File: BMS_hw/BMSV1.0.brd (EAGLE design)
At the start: 272 x 60 mm, 161 parts, among them IC1 MC33771BEP, IC2 SFH6156, J2 NTC, X2 87758-1816

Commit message: updated after nxp review
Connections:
- removed net N$28: C67.1, IC1.43
- new net N$14: IC1.45, IC1.48
- net GND: no longer R66.2
- net VCOM: now also C67.1, IC1.43, R66.2
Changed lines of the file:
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@@
 <contactref element="C67" pad="2"/>
 <contactref element="IC2" pad="2"/>
-<contactref element="R66" pad="2"/>
 <contactref element="R67" pad="2"/>
 <contactref element="X2" pad="11"/>
@@
 <wire x1="-96.94" y1="19.05" x2="-81.7" y2="38.1" width="0" layer="19" extent="1-1"/>
 <wire x1="-30.75" y1="76.2" x2="-48.68" y2="50.8" width="0" layer="19" extent="1-1"/>
-<wire x1="-25.67" y1="76.2" x2="-30.75" y2="76.2" width="0" layer="19" extent="1-1"/>
 <wire x1="29.27" y1="36.41" x2="-18.2" y2="25.4" width="0" layer="19" extent="1-1"/>
 <wire x1="-20.825" y1="-100.33" x2="-79.58" y2="-95.25" width="0" layer="19" extent="1-1"/>
@@
 <contactref element="R97" pad="2"/>
 <contactref element="R98" pad="2"/>
+<contactref element="C67" pad="1"/>
+<contactref element="IC1" pad="43"/>
+<contactref element="R66" pad="2"/>
 <wire x1="-75.2" y1="-68.58" x2="-80.28" y2="-68.58" width="0" layer="19" extent="1-1"/>
 <wire x1="-70.12" y1="-68.58" x2="-75.2" y2="-68.58" width="0" layer="19" extent="1-1"/>
@@
 <wire x1="-54.88" y1="-68.58" x2="-59.96" y2="-68.58" width="0" layer="19" extent="1-1"/>
 <wire x1="-49.8" y1="-68.58" x2="-54.88" y2="-68.58" width="0" layer="19" extent="1-1"/>
+<wire x1="-56.73" y1="50.8" x2="-54.88" y2="-68.58" width="0" layer="19" extent="1-1"/>
+<wire x1="-25.67" y1="76.2" x2="-56.73" y2="50.8" width="0" layer="19" extent="1-1"/>
+<wire x1="38.95" y1="31.73" x2="-25.67" y2="76.2" width="0" layer="19" extent="1-1"/>
 </signal>
 <signal name="GPIO0">
@@
 <contactref element="C66" pad="1"/>
 <wire x1="-50.38" y1="50.8" x2="31.27" y2="36.41" width="0" layer="19" extent="1-1"/>
-</signal>
-<signal name="N$28">
-<contactref element="C67" pad="1"/>
-<contactref element="IC1" pad="43"/>
-<wire x1="-56.73" y1="50.8" x2="38.95" y2="31.73" width="0" layer="19" extent="1-1"/>
 </signal>
 <signal name="VPWR">
@@
 <contactref element="R7" pad="1"/>
 </signal>
+<signal name="N$14">
+<contactref element="IC1" pad="45"/>
+<contactref element="IC1" pad="48"/>
+<wire x1="38.95" y1="32.73" x2="38.95" y2="34.23" width="0" layer="19" extent="1-1"/>
+</signal>
 </signals>

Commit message: cell terminal pads are placed according to design
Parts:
- CELL1+, CELL1-, CELL10+, CELL11+, CELL12+, CELL13+, CELL14+, CELL2+, CELL3+, CELL4+, CELL5+, CELL6+, CELL7+, CELL8+, CELL9+: value TPSQTP20SQ -> GF_BMS_CELL_PADP_PAD; device testpad:TP20SQ -> GreenFuel:GF-BMS-PAD
- moved CELL14+ 329.2 mm to (259.5, 54.0)
- moved CELL13+ 309.5 mm to (240.5, 6.00)
- moved CELL12+ 292.6 mm to (240.5, 54.0)
- moved CELL11+ 289.9 mm to (202.5, 6.00)
- moved CELL8+ 265.7 mm to (164.5, 54.0)
- moved CELL6+ 257.6 mm to (126.5, 54.0)
- moved CELL10+ 245.9 mm to (202.5, 54.0)
- moved CELL7+ 227.7 mm to (126.5, 6.00)
- moved CELL5+ 209.2 mm to (88.5, 6.00)
- moved CELL9+ 203.0 mm to (164.5, 6.00)
- moved CELL4+ 188.9 mm to (88.5, 54.0)
- moved CELL2+ 174.6 mm to (50.5, 54.0)
- moved CELL1- 161.1 mm to (12.5, 54.0)
- moved CELL3+ 135.7 mm to (50.5, 6.00)
- moved CELL1+ 120.1 mm to (12.5, 6.00)
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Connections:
- net CB_10/9_C: now also CELL9+.1; no longer CELL9+.TP
- net CB_12/11_C: now also CELL11+.1; no longer CELL11+.TP
- net CB_13/12_C: now also CELL12+.1; no longer CELL12+.TP
- net CB_13/12_C1: now also CELL10+.1; no longer CELL10+.TP
- net CB_13/12_C2: now also CELL8+.1; no longer CELL8+.TP
- net CB_13/12_C6: now also CELL6+.1; no longer CELL6+.TP
- net CB_13/12_C7: now also CELL4+.1; no longer CELL4+.TP
- net CB_13/12_C8: now also CELL2+.1; no longer CELL2+.TP
- net CB_14/13_C: now also CELL13+.1; no longer CELL13+.TP
- net CB_2/1_C: now also CELL1+.1; no longer CELL1+.TP
- net CB_4/3_C: now also CELL3+.1; no longer CELL3+.TP
- net CB_6/5_C: now also CELL5+.1; no longer CELL5+.TP
- net CB_8/7_C: now also CELL7+.1; no longer CELL7+.TP
- net CELL1-: now also CELL1-.1; no longer CELL1-.TP
- net CELL14+: now also CELL14+.1; no longer CELL14+.TP
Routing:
- added copper zone on layer 16, net GND

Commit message: board updated cell name and value
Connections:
- net CB_10/9_C: now also CELL9+.P$1; no longer CELL9+.1
- net CB_12/11_C: now also CELL11+.P$1; no longer CELL11+.1
- net CB_13/12_C: now also CELL12+.P$1; no longer CELL12+.1
- net CB_13/12_C1: now also CELL10+.P$1; no longer CELL10+.1
- net CB_13/12_C2: now also CELL8+.P$1; no longer CELL8+.1
- net CB_13/12_C6: now also CELL6+.P$1; no longer CELL6+.1
- net CB_13/12_C7: now also CELL4+.P$1; no longer CELL4+.1
- net CB_13/12_C8: now also CELL2+.P$1; no longer CELL2+.1
- net CB_14/13_C: now also CELL13+.P$1; no longer CELL13+.1
- net CB_2/1_C: now also CELL1+.P$1; no longer CELL1+.1
- net CB_4/3_C: now also CELL3+.P$1; no longer CELL3+.1
- net CB_6/5_C: now also CELL5+.P$1; no longer CELL5+.1
- net CB_8/7_C: now also CELL7+.P$1; no longer CELL7+.1
- net CELL1-: now also CELL1-.P$1; no longer CELL1-.1
- net CELL14+: now also CELL14+.P$1; no longer CELL14+.1
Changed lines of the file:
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@@
 </elements>
 <signals>
-<signal name="N$1">
-<contactref element="R26" pad="2"/>
-<contactref element="R31" pad="1"/>
-<contactref element="C27" pad="1"/>
-<wire x1="-42.76" y1="44.45" x2="-91.71" y2="57.15" width="0" layer="19" extent="1-1"/>
-<wire x1="-32.75" y1="63.5" x2="-42.76" y2="44.45" width="0" layer="19" extent="1-1"/>
-</signal>
 <signal name="GND">
 <contactref element="C27" pad="2"/>
@@
 <contactref element="C20" pad="2"/>
 <contactref element="C4" pad="2"/>
-<contactref element="C21" pad="2"/>
 <contactref element="IC1" pad="65"/>
 <contactref element="IC1" pad="58"/>
@@
 <vertex x="0" y="48"/>
 </polygon>
+<contactref element="C21" pad="2"/>
 <wire x1="-94.4" y1="-107.95" x2="-100.75" y2="-107.95" width="0" layer="19" extent="1-1"/>
 <wire x1="-88.05" y1="-107.95" x2="-94.4" y2="-107.95" width="0" layer="19" extent="1-1"/>
@@
 <contactref element="C10" pad="1"/>
 <contactref element="R17" pad="1"/>
-<contactref element="CELL13+" pad="1"/>
+<contactref element="CELL13+" pad="P$1"/>
 <wire x1="-37.68" y1="25.4" x2="240.5" y2="6" width="0" layer="19" extent="1-1"/>
 <wire x1="-47.99" y1="57.15" x2="-37.68" y2="25.4" width="0" layer="19" extent="1-1"/>
@@
 <contactref element="R6" pad="1"/>
 <contactref element="R9" pad="1"/>
-<contactref element="CELL12+" pad="1"/>
+<contactref element="CELL12+" pad="P$1"/>
 <wire x1="-22.59" y1="82.55" x2="-17.51" y2="82.55" width="0" layer="19" extent="1-1"/>
 <wire x1="-63.08" y1="19.05" x2="-22.59" y2="82.55" width="0" layer="19" extent="1-1"/>
@@
 <contactref element="C11" pad="1"/>
 <contactref element="R18" pad="1"/>
-<contactref element="CELL11+" pad="1"/>
+<contactref element="CELL11+" pad="P$1"/>
 <contactref element="IC1" pad="10"/>
 <wire x1="39.91" y1="29.73" x2="202.5" y2="6" width="0" layer="19" extent="1-16"/>
@@
 <contactref element="R4" pad="1"/>
 <contactref element="R14" pad="1"/>
-<contactref element="CELL10+" pad="1"/>
+<contactref element="CELL10+" pad="P$1"/>
 <wire x1="-32.75" y1="57.15" x2="-17.51" y2="63.5" width="0" layer="19" extent="1-1"/>
 <wire x1="-19.9" y1="25.4" x2="-32.75" y2="57.15" width="0" layer="19" extent="1-1"/>
@@
 <wire x1="-51.07" y1="63.5" x2="-37.68" y2="31.75" width="0" layer="19" extent="1-1"/>
 </signal>
-<signal name="N$8">
-<contactref element="R20" pad="2"/>
-<contactref element="R37" pad="1"/>
-<contactref element="C21" pad="1"/>
-<wire x1="-61.23" y1="57.15" x2="-83.4" y2="38.1" width="0" layer="19" extent="1-1"/>
-<wire x1="-63.23" y1="63.5" x2="-61.23" y2="57.15" width="0" layer="19" extent="1-1"/>
-</signal>
 <signal name="CB_13/12_C2">
 <contactref element="C4" pad="1"/>
@@
 <contactref element="R2" pad="1"/>
 <contactref element="R10" pad="1"/>
-<contactref element="CELL8+" pad="1"/>
+<contactref element="CELL8+" pad="P$1"/>
 <wire x1="-17.51" y1="57.15" x2="164.5" y2="54" width="0" layer="19" extent="1-1"/>
 <wire x1="-63.23" y1="57.15" x2="-17.51" y2="57.15" width="0" layer="19" extent="1-1"/>
@@
 </signal>
 <signal name="CT_8">
+<contactref element="C36" pad="2"/>
+<contactref element="IC1" pad="18"/>
 <contactref element="R37" pad="2"/>
 <contactref element="C37" pad="1"/>
-<contactref element="C36" pad="2"/>
-<contactref element="IC1" pad="18"/>
 <wire x1="-44.87" y1="31.75" x2="37.23" y2="24.55" width="0" layer="19" extent="1-16"/>
 <wire x1="-55.46" y1="31.75" x2="-44.87" y2="31.75" width="0" layer="19" extent="1-1"/>
@@
 <contactref element="C71" pad="1"/>
 <contactref element="R46" pad="1"/>
-<contactref element="CELL7+" pad="1"/>
+<contactref element="CELL7+" pad="P$1"/>
 <contactref element="D10" pad="A"/>
 <wire x1="-77.2" y1="-55.88" x2="-99.9" y2="-95.25" width="0" layer="19" extent="1-1"/>
@@
 </signal>
 <signal name="CT_7">
+<contactref element="IC1" pad="22"/>
 <contactref element="C37" pad="2"/>
-<contactref element="IC1" pad="22"/>
 <wire x1="-53.76" y1="31.75" x2="35.23" y2="24.55" width="0" layer="19" extent="1-16"/>
 </signal>
@@
 <contactref element="C75" pad="1"/>
 <contactref element="R73" pad="1"/>
-<contactref element="CELL5+" pad="1"/>
+<contactref element="CELL5+" pad="P$1"/>
 <wire x1="-60.54" y1="-21.59" x2="-56.88" y2="-55.88" width="0" layer="19" extent="1-1"/>
 <wire x1="33.73" y1="24.55" x2="-60.54" y2="-21.59" width="0" layer="19" extent="1-16"/>
@@
 <contactref element="C12" pad="1"/>
 <contactref element="R19" pad="1"/>
-<contactref element="CELL9+" pad="1"/>
+<contactref element="CELL9+" pad="P$1"/>
 <contactref element="IC1" pad="15"/>
 <contactref element="D11" pad="A"/>
@@
 <contactref element="C81" pad="1"/>
 <contactref element="R79" pad="1"/>
-<contactref element="CELL3+" pad="1"/>
+<contactref element="CELL3+" pad="P$1"/>
 <wire x1="-84.67" y1="-30.48" x2="-87.36" y2="-62.23" width="0" layer="19" extent="1-1"/>
 <wire x1="31.23" y1="24.55" x2="-84.67" y2="-30.48" width="0" layer="19" extent="1-16"/>
@@
 <contactref element="C87" pad="1"/>
 <contactref element="R85" pad="1"/>
-<contactref element="CELL1+" pad="1"/>
+<contactref element="CELL1+" pad="P$1"/>
 <wire x1="-49.11" y1="-30.48" x2="-56.88" y2="-62.23" width="0" layer="19" extent="1-1"/>
 <wire x1="12.5" y1="6" x2="-49.11" y2="-30.48" width="0" layer="19" extent="1-1"/>
@@
 <contactref element="C91" pad="1"/>
 <contactref element="R89" pad="1"/>
-<contactref element="CELL1-" pad="1"/>
+<contactref element="CELL1-" pad="P$1"/>
 <contactref element="R91" pad="1"/>
 <contactref element="C9" pad="1"/>
@@
 </signal>
 <signal name="CELL14+">
-<contactref element="CELL14+" pad="1"/>
 <contactref element="R26" pad="1"/>
+<contactref element="R1" pad="1"/>
+<contactref element="CELL14+" pad="P$1"/>
 <contactref element="C7" pad="1"/>
 <contactref element="R13" pad="2"/>
-<contactref element="R1" pad="1"/>
 <wire x1="-98.64" y1="19.05" x2="-97.52" y2="-114.3" width="0" layer="19" extent="1-1"/>
 <wire x1="-93.71" y1="57.15" x2="-98.64" y2="19.05" width="0" layer="19" extent="1-1"/>
@@
 <contactref element="R75" pad="1"/>
 <contactref element="R76" pad="1"/>
-<contactref element="CELL6+" pad="1"/>
+<contactref element="CELL6+" pad="P$1"/>
 <wire x1="-46.72" y1="-55.88" x2="126.5" y2="54" width="0" layer="19" extent="1-1"/>
 <wire x1="-67.04" y1="-55.88" x2="-46.72" y2="-55.88" width="0" layer="19" extent="1-1"/>
@@
 <contactref element="R81" pad="1"/>
 <contactref element="R82" pad="1"/>
-<contactref element="CELL4+" pad="1"/>
+<contactref element="CELL4+" pad="P$1"/>
 <wire x1="-77.2" y1="-62.23" x2="-97.52" y2="-62.23" width="0" layer="19" extent="1-1"/>
 <wire x1="-72.12" y1="-62.23" x2="-77.2" y2="-62.23" width="0" layer="19" extent="1-1"/>
@@
 <contactref element="R87" pad="1"/>
 <contactref element="R88" pad="1"/>
-<contactref element="CELL2+" pad="1"/>
+<contactref element="CELL2+" pad="P$1"/>
 <wire x1="-67.04" y1="-62.23" x2="-102.6" y2="-68.58" width="0" layer="19" extent="1-1"/>
 <wire x1="-46.72" y1="-62.23" x2="-67.04" y2="-62.23" width="0" layer="19" extent="1-1"/>
@@
 <wire x1="28.05" y1="32.73" x2="28.05" y2="34.23" width="0" layer="19" extent="16-16"/>
 </signal>
+<signal name="N$2">
+<contactref element="R20" pad="2"/>
+<contactref element="R37" pad="1"/>
+<contactref element="C21" pad="1"/>
+<wire x1="-61.23" y1="57.15" x2="-83.4" y2="38.1" width="0" layer="19" extent="1-1"/>
+<wire x1="-63.23" y1="63.5" x2="-61.23" y2="57.15" width="0" layer="19" extent="1-1"/>
+</signal>
+<signal name="N$1">
+<contactref element="R26" pad="2"/>
+<contactref element="R31" pad="1"/>
+<contactref element="C27" pad="1"/>
+<wire x1="-42.76" y1="44.45" x2="-91.71" y2="57.15" width="0" layer="19" extent="1-1"/>
+<wire x1="-32.75" y1="63.5" x2="-42.76" y2="44.45" width="0" layer="19" extent="1-1"/>
+</signal>
 </signals>

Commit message: gf_bms_ hw v1.0 board layout names and values changed
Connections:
- removed net N$14: IC1.45, IC1.48
- net GND: now also IC1.45, IC1.48
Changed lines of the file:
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@@
 </polygon>
 <contactref element="C21" pad="2"/>
+<contactref element="IC1" pad="45"/>
+<contactref element="IC1" pad="48"/>
 <wire x1="-94.4" y1="-107.95" x2="-100.75" y2="-107.95" width="0" layer="19" extent="1-1"/>
 <wire x1="-88.05" y1="-107.95" x2="-94.4" y2="-107.95" width="0" layer="19" extent="1-1"/>
@@
 <wire x1="-30.75" y1="76.2" x2="-48.68" y2="50.8" width="0" layer="19" extent="1-1"/>
 <wire x1="28.05" y1="32.23" x2="-18.2" y2="25.4" width="0" layer="19" extent="1-16"/>
+<wire x1="28.05" y1="32.73" x2="28.05" y2="32.23" width="0" layer="19" extent="16-16"/>
+<wire x1="28.05" y1="34.23" x2="28.05" y2="32.73" width="0" layer="19" extent="16-16"/>
 <wire x1="33.98" y1="30.48" x2="28.05" y2="32.23" width="0" layer="19" extent="16-16"/>
 <wire x1="34.73" y1="36.41" x2="33.98" y2="30.48" width="0" layer="19" extent="16-16"/>
@@
 <contactref element="C11" pad="1"/>
 <contactref element="R18" pad="1"/>
+<contactref element="IC1" pad="10"/>
 <contactref element="CELL11+" pad="P$1"/>
-<contactref element="IC1" pad="10"/>
 <wire x1="39.91" y1="29.73" x2="202.5" y2="6" width="0" layer="19" extent="1-16"/>
 <wire x1="-46.57" y1="25.4" x2="39.91" y2="29.73" width="0" layer="19" extent="1-16"/>
@@
 <contactref element="C12" pad="1"/>
 <contactref element="R19" pad="1"/>
-<contactref element="CELL9+" pad="P$1"/>
 <contactref element="IC1" pad="15"/>
 <contactref element="D11" pad="A"/>
+<contactref element="CELL9+" pad="P$1"/>
 <wire x1="-55.46" y1="25.4" x2="-94.82" y2="-95.25" width="0" layer="19" extent="1-1"/>
 <wire x1="-58.15" y1="57.15" x2="-55.46" y2="25.4" width="0" layer="19" extent="1-1"/>
@@
 <contactref element="R7" pad="1"/>
 </signal>
-<signal name="N$14">
-<contactref element="IC1" pad="45"/>
-<contactref element="IC1" pad="48"/>
-<wire x1="28.05" y1="32.73" x2="28.05" y2="34.23" width="0" layer="19" extent="16-16"/>
-</signal>
 <signal name="N$2">

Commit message: hot plug protection and filters board regrid done !
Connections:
- removed net N$10: C5.1, D15.C, R3.1
- new net N$14: C9.1, R7.2, R8.2
- new net N$15: D17.C, R5.1
- net CELL1-: no longer C9.1, D17.C, R5.1
- net GND: no longer R7.2
- net V-: now also C5.1, D15.C, R3.1, R8.1
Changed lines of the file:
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@@
 <contactref element="C76" pad="2"/>
 <contactref element="C79" pad="2"/>
-<contactref element="C80" pad="2"/>
 <contactref element="C81" pad="2"/>
 <contactref element="C82" pad="2"/>
@@
 <contactref element="C13" pad="2"/>
 <contactref element="IC1" pad="44"/>
-<contactref element="R7" pad="2"/>
 <polygon width="0.4064" layer="16" isolate="0.4064">
 <vertex x="0" y="0"/>
@@
 <contactref element="IC1" pad="45"/>
 <contactref element="IC1" pad="48"/>
+<contactref element="C80" pad="2"/>
 <wire x1="-94.4" y1="-107.95" x2="-100.75" y2="-107.95" width="0" layer="19" extent="1-1"/>
 <wire x1="-88.05" y1="-107.95" x2="-94.4" y2="-107.95" width="0" layer="19" extent="1-1"/>
@@
 <wire x1="37.73" y1="36.41" x2="35.23" y2="36.41" width="0" layer="19" extent="16-16"/>
 <wire x1="64.77" y1="36.83" x2="37.73" y2="36.41" width="0" layer="19" extent="1-16"/>
-<wire x1="-20.825" y1="-100.33" x2="-79.58" y2="-95.25" width="0" layer="19" extent="1-1"/>
 </signal>
 <signal name="CB_14">
@@
 <contactref element="C71" pad="1"/>
 <contactref element="R46" pad="1"/>
+<contactref element="D10" pad="A"/>
 <contactref element="CELL7+" pad="P$1"/>
-<contactref element="D10" pad="A"/>
 <wire x1="-77.2" y1="-55.88" x2="-99.9" y2="-95.25" width="0" layer="19" extent="1-1"/>
 <wire x1="-78.32" y1="-21.59" x2="-77.2" y2="-55.88" width="0" layer="19" extent="1-1"/>
@@
 <contactref element="C91" pad="1"/>
 <contactref element="R89" pad="1"/>
+<contactref element="R91" pad="1"/>
 <contactref element="CELL1-" pad="P$1"/>
-<contactref element="R91" pad="1"/>
-<contactref element="C9" pad="1"/>
-<contactref element="D17" pad="C"/>
-<contactref element="R5" pad="1"/>
-<wire x1="-98.22" y1="-101.6" x2="-102.6" y2="-114.3" width="0" layer="19" extent="1-1"/>
-<wire x1="-89.75" y1="-107.95" x2="-98.22" y2="-101.6" width="0" layer="19" extent="1-1"/>
-<wire x1="-97.52" y1="-68.58" x2="-98.22" y2="-101.6" width="0" layer="19" extent="1-1"/>
 <wire x1="-87.36" y1="-68.58" x2="-97.52" y2="-68.58" width="0" layer="19" extent="1-1"/>
 <wire x1="-84.67" y1="-36.83" x2="-87.36" y2="-68.58" width="0" layer="19" extent="1-1"/>
@@
 <wire x1="-102.6" y1="-62.23" x2="-67.04" y2="-55.88" width="0" layer="19" extent="1-1"/>
 </signal>
-<signal name="N$43">
-<contactref element="R73" pad="2"/>
-<contactref element="R74" pad="1"/>
-<contactref element="C76" pad="1"/>
-<wire x1="-54.88" y1="-55.88" x2="-102.45" y2="-43.18" width="0" layer="19" extent="1-1"/>
-<wire x1="-51.8" y1="-55.88" x2="-54.88" y2="-55.88" width="0" layer="19" extent="1-1"/>
-</signal>
 <signal name="N$44">
 <contactref element="R77" pad="2"/>
@@
 <wire x1="-74.5" y1="-95.25" x2="-99.9" y2="-101.6" width="0" layer="19" extent="1-1"/>
 </signal>
-<signal name="N$10">
+<signal name="N$11">
+<contactref element="D18" pad="A"/>
+<contactref element="D17" pad="A"/>
+<wire x1="-89.74" y1="-101.6" x2="-94.82" y2="-101.6" width="0" layer="19" extent="1-1"/>
+</signal>
+<signal name="MISO">
+<contactref element="IC1" pad="42"/>
+</signal>
+<signal name="MOSI">
+<contactref element="IC1" pad="47"/>
+</signal>
+<signal name="SCLK">
+<contactref element="IC1" pad="46"/>
+</signal>
+<signal name="V-">
+<contactref element="R7" pad="1"/>
+<contactref element="R8" pad="1"/>
 <contactref element="D15" pad="C"/>
 <contactref element="R3" pad="1"/>
@@
 <wire x1="-96.1" y1="-107.95" x2="-92.44" y2="-114.3" width="0" layer="19" extent="1-1"/>
 <wire x1="-77.9" y1="-95.25" x2="-96.1" y2="-107.95" width="0" layer="19" extent="1-1"/>
-</signal>
-<signal name="N$11">
-<contactref element="D18" pad="A"/>
-<contactref element="D17" pad="A"/>
-<wire x1="-89.74" y1="-101.6" x2="-94.82" y2="-101.6" width="0" layer="19" extent="1-1"/>
-</signal>
-<signal name="MISO">
-<contactref element="IC1" pad="42"/>
-</signal>
-<signal name="MOSI">
-<contactref element="IC1" pad="47"/>
-</signal>
-<signal name="SCLK">
-<contactref element="IC1" pad="46"/>
-</signal>
-<signal name="V-">
-<contactref element="R7" pad="1"/>
+<wire x1="-29.975" y1="-100.33" x2="-77.9" y2="-95.25" width="0" layer="19" extent="1-1"/>
+<wire x1="-18.545" y1="-83.82" x2="-29.975" y2="-100.33" width="0" layer="19" extent="1-1"/>
 </signal>
 <signal name="N$2">
@@
 <wire x1="-32.75" y1="63.5" x2="-42.76" y2="44.45" width="0" layer="19" extent="1-1"/>
 </signal>
+<signal name="N$8">
+<contactref element="R73" pad="2"/>
+<contactref element="R74" pad="1"/>
+<contactref element="C76" pad="1"/>
+<wire x1="-54.88" y1="-55.88" x2="-102.45" y2="-43.18" width="0" layer="19" extent="1-1"/>
+<wire x1="-51.8" y1="-55.88" x2="-54.88" y2="-55.88" width="0" layer="19" extent="1-1"/>
+</signal>
+<signal name="N$15">
+<contactref element="D17" pad="C"/>
+<contactref element="R5" pad="1"/>
+<wire x1="-98.22" y1="-101.6" x2="-102.6" y2="-114.3" width="0" layer="19" extent="1-1"/>
+</signal>
+<signal name="N$14">
+<contactref element="R7" pad="2"/>
+<contactref element="R8" pad="2"/>
+<contactref element="C9" pad="1"/>
+<wire x1="-20.825" y1="-100.33" x2="-89.75" y2="-107.95" width="0" layer="19" extent="1-1"/>
+<wire x1="-9.395" y1="-83.82" x2="-20.825" y2="-100.33" width="0" layer="19" extent="1-1"/>
+</signal>
 </signals>

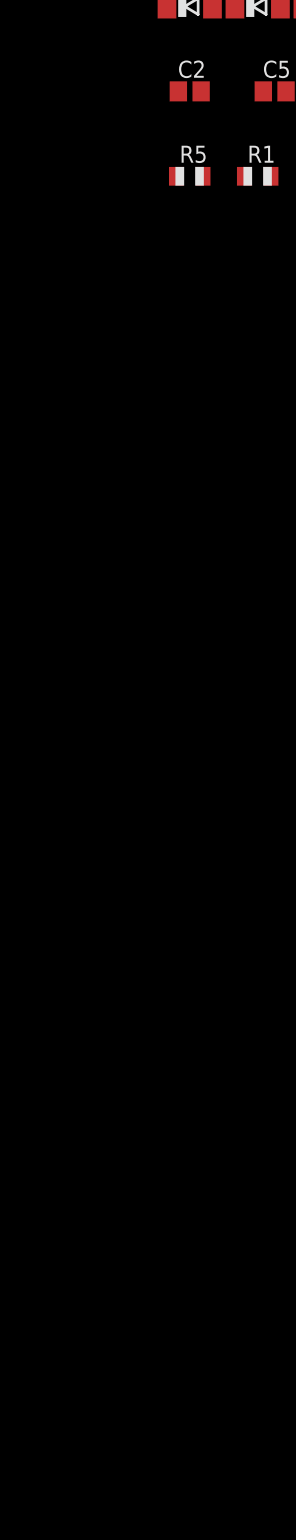
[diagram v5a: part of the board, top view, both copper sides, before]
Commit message: buck convertor is added to board layout
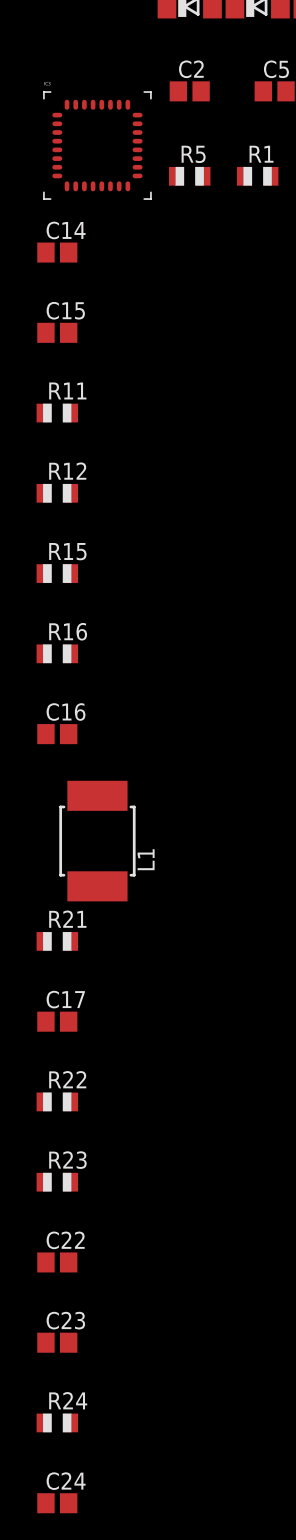
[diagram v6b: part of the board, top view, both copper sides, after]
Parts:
- added C14, C15, C16, C17, C22, C23, C24: 47nF, adafruit:C0805
- added IC3: MIC28515V1, GreenFuel:VQFN-32
- added L1: (no value), inductor-neosid:MS85
- added R11, R12, R15, R16, R21, R22, R23, R24: 127E, adafruit:R0805
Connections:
- new net BST: C24.1
- new net FB: C17.2, IC3.27
- new net ILIM: R24.1
- new net N$10: C14.1, IC3.30, R11.2
- new net N$16: C15.1, IC3.21, R11.1
- new net N$17: IC3.25, R12.1, R15.1
- new net N$18: C16.1, IC3.23
- new net N$19: IC3.1, R16.1
- new net N$20: IC3.12, IC3.13, IC3.14, IC3.15, IC3.3, R16.2
- new net N$21: C22.1, C23.1, L1.2, R22.1
- new net N$22: R22.2, R23.1
- new net N$24: C17.1, R21.2
- new net PGND: IC3.16, IC3.17, IC3.18, IC3.19, IC3.2, IC3.22, IC3.29
- new net SW: C24.2, IC3.20, L1.1, R21.1, R24.2
- new net VIN: IC3.10, IC3.11, IC3.5, IC3.6, IC3.7, IC3.8, IC3.9, R12.2
- net AGND: now also IC3.28
- net GND: now also C14.2, C15.2, C16.2, C22.2, C23.2, R15.2, R23.2
